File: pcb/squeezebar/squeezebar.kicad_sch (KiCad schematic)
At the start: 44 parts, among them J2 Conn_02x08_Counter_Clockwise, U1 Elite-C

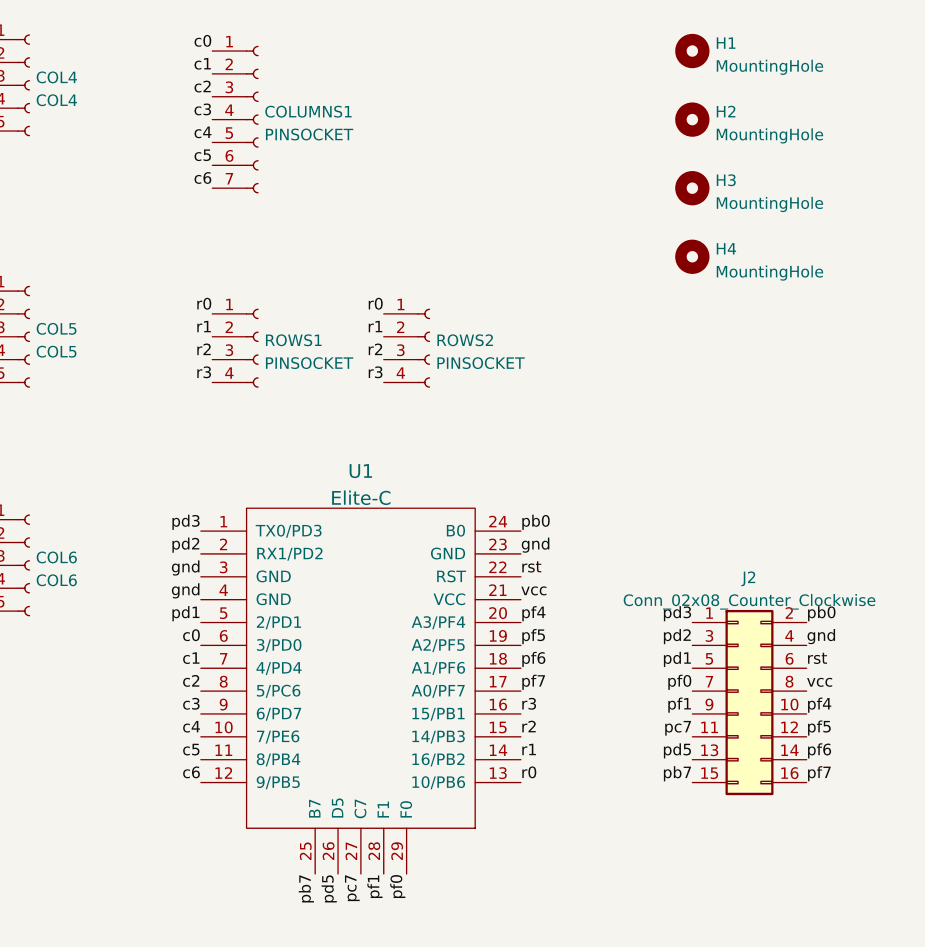
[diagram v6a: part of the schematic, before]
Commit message: Reassign pins; break out I²C & RST at the expense of 2 mounting holes
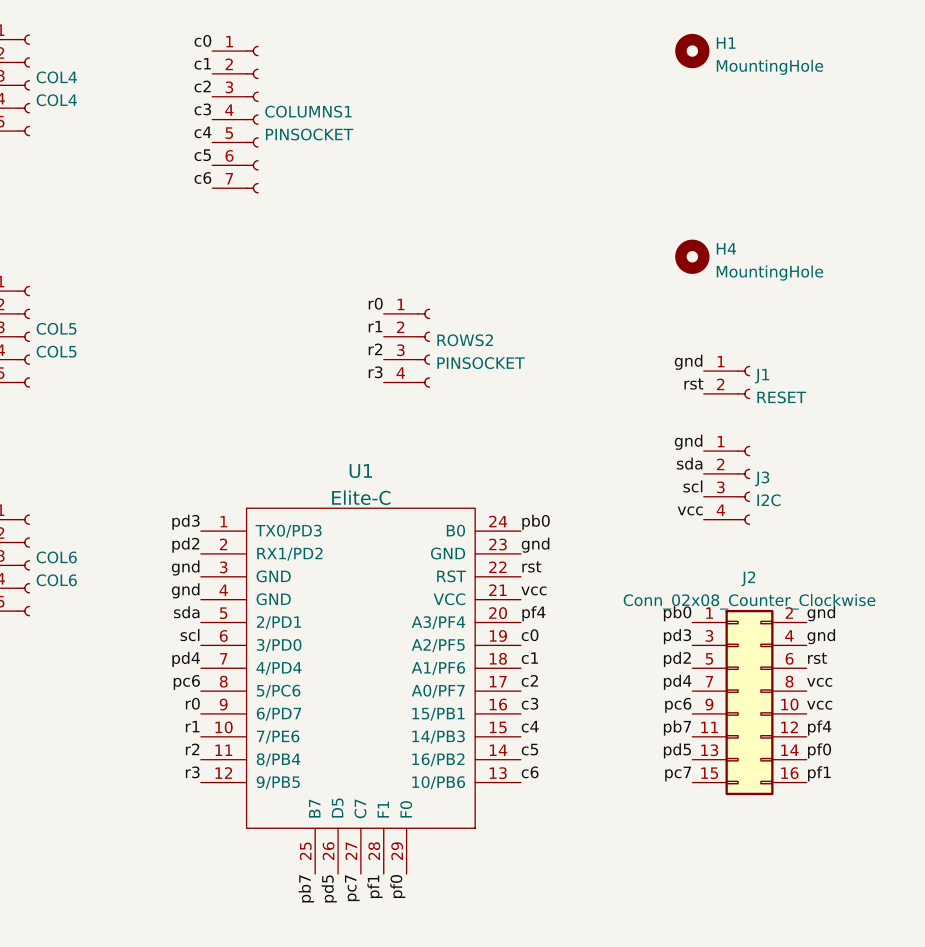
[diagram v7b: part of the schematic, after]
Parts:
- removed H2, H3: MountingHole, symbol Mechanical:MountingHole
- removed ROWS1: PINSOCKET, Library:PinSocket_1x04_P2.54mm_Vertical_LongPads, symbol Connector:Conn_01x04_Female
- added J1: RESET, Library:PinHeader_RST_1x02_P2.54mm_Vertical, symbol Connector:Conn_01x02_Female
- added J3: I2C, Library:PinHeader_I2C_1x04_P2.54mm_Vertical, symbol Connector:Conn_01x04_Female
- COL0, COL1, COL2, COL3, COL4, COL5, COL6: footprint Library:PinHeader_1x05_P2.54mm_Vertical -> Library:PinHeader_Col_1x05_P2.54mm_Vertical
- COLUMNS1: footprint Connector_PinHeader_2.54mm:PinHeader_1x07_P2.54mm_Vertical -> Library:PinHeader_COLS_1x07_P2.54mm_Vertical
- H1, H4: footprint (none) -> MountingHole:MountingHole_3.2mm_M3_DIN965
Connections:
- net c0: now also U1.19 (A2/PF5); no longer U1.6 (3/PD0)
- net c1: now also U1.18 (A1/PF6); no longer U1.7 (4/PD4)
- net c2: now also U1.17 (A0/PF7); no longer U1.8 (5/PC6)
- net c3: now also U1.16 (15/PB1); no longer U1.9 (6/PD7)
- net c4: now also U1.15 (14/PB3); no longer U1.10 (7/PE6)
- net c5: now also U1.14 (16/PB2); no longer U1.11 (8/PB4)
- net c6: now also U1.13 (10/PB6); no longer U1.12 (9/PB5)
- net gnd: now also J2.2 (Pin_2), J1.1 (Pin_1), J3.1 (Pin_1)
- net pb0: now also J2.1 (Pin_1); no longer J2.2 (Pin_2)
- net pb7: now also J2.11 (Pin_11); no longer J2.15 (Pin_15)
- net pc7: now also J2.15 (Pin_15); no longer J2.11 (Pin_11)
- net pd2: now also J2.5 (Pin_5); no longer J2.3 (Pin_3)
- net pd3: now also J2.3 (Pin_3); no longer J2.1 (Pin_1)
- net pf0: now also J2.14 (Pin_14); no longer J2.7 (Pin_7)
- net pf1: now also J2.16 (Pin_16); no longer J2.9 (Pin_9)
- net pf4: now also J2.12 (Pin_12); no longer J2.10 (Pin_10)
- net r0: now also U1.9 (6/PD7); no longer U1.13 (10/PB6)
- net r1: now also U1.10 (7/PE6); no longer U1.14 (16/PB2)
- net r2: now also U1.11 (8/PB4); no longer U1.15 (14/PB3)
- net r3: now also U1.12 (9/PB5); no longer U1.16 (15/PB1)
- net rst: now also J1.2 (Pin_2)
- net vcc: now also J2.10 (Pin_10), J3.4 (Pin_4)
- net pd1 renamed sda
- net sda: now also J3.2 (Pin_2); no longer J2.5 (Pin_5)
- removed net pf5: J2.12 (Pin_12), U1.19 (A2/PF5)
- removed net pf6: J2.14 (Pin_14), U1.18 (A1/PF6)
- removed net pf7: J2.16 (Pin_16), U1.17 (A0/PF7)
- new net pc6: J2.9 (Pin_9), U1.8 (5/PC6)
- new net pd4: J2.7 (Pin_7), U1.7 (4/PD4)
- new net scl: J3.3 (Pin_3), U1.6 (3/PD0)

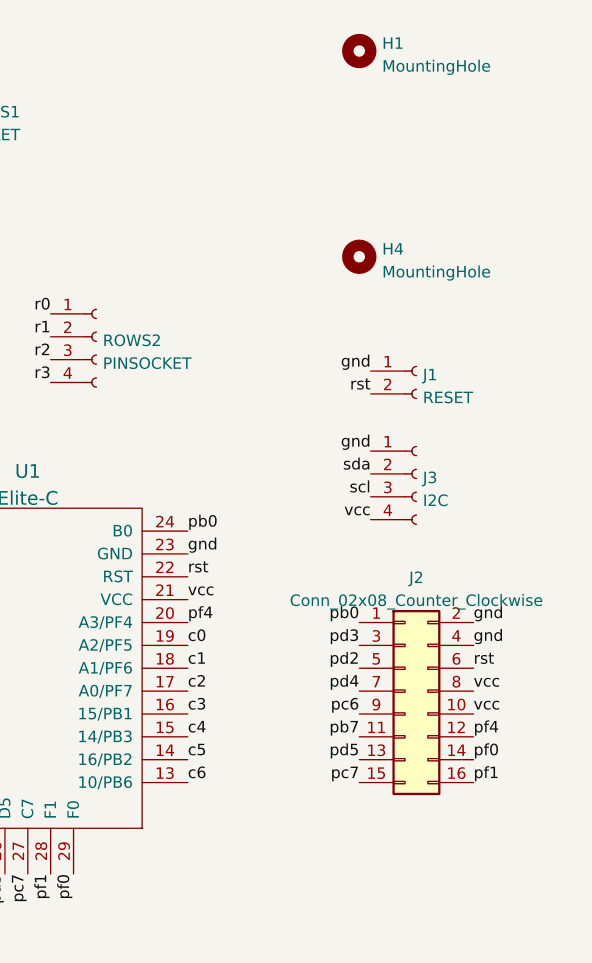
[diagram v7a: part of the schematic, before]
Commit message: Move mounting hole from under the MCU
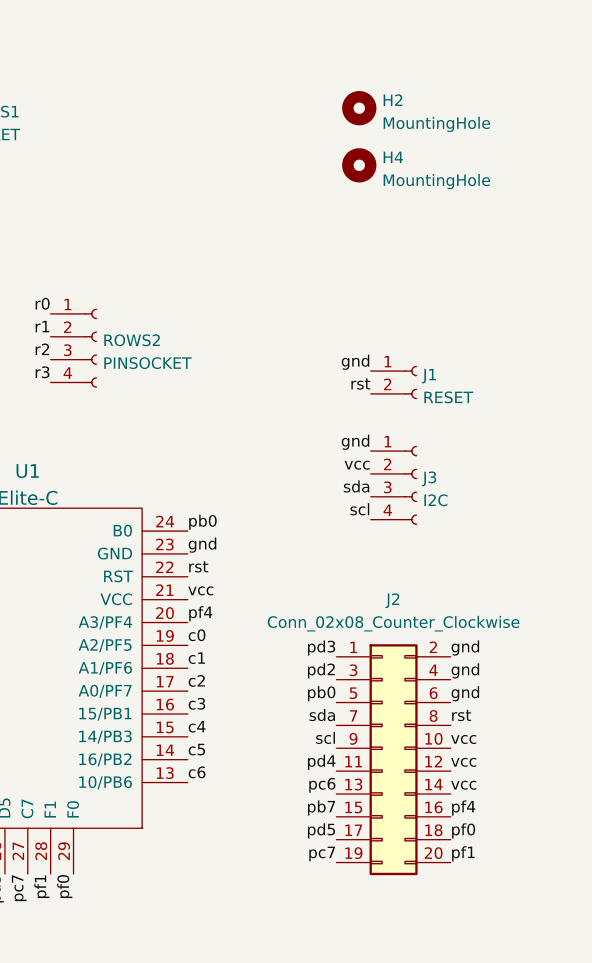
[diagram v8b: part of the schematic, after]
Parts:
- removed H1: MountingHole, MountingHole:MountingHole_3.2mm_M3_DIN965, symbol Mechanical:MountingHole
- added H2: MountingHole, MountingHole:MountingHole_3.2mm_M3_DIN965, symbol Mechanical:MountingHole
- J2: footprint Library:PinSocket_2x08_P2.54mm_Bespoke -> Connector_PinSocket_2.54mm:PinSocket_2x10_P2.54mm_Vertical; symbol Connector_Generic:Conn_02x08_Odd_Even -> Connector_Generic:Conn_02x10_Odd_Even
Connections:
- net gnd: now also J2.6 (Pin_6)
- net pb0: now also J2.5 (Pin_5); no longer J2.1 (Pin_1)
- net pb7: now also J2.15 (Pin_15); no longer J2.11 (Pin_11)
- net pc6: now also J2.13 (Pin_13); no longer J2.9 (Pin_9)
- net pc7: now also J2.19 (Pin_19); no longer J2.15 (Pin_15)
- net pd2: now also J2.3 (Pin_3); no longer J2.5 (Pin_5)
- net pd3: now also J2.1 (Pin_1); no longer J2.3 (Pin_3)
- net pd4: now also J2.11 (Pin_11); no longer J2.7 (Pin_7)
- net pd5: now also J2.17 (Pin_17); no longer J2.13 (Pin_13)
- net pf0: now also J2.18 (Pin_18); no longer J2.14 (Pin_14)
- net pf1: now also J2.20 (Pin_20); no longer J2.16 (Pin_16)
- net pf4: now also J2.16 (Pin_16); no longer J2.12 (Pin_12)
- net rst: now also J2.8 (Pin_8); no longer J2.6 (Pin_6)
- net scl: now also J2.9 (Pin_9), J3.4 (Pin_4); no longer J3.3 (Pin_3)
- net sda: now also J2.7 (Pin_7), J3.3 (Pin_3); no longer J3.2 (Pin_2)
- net vcc: now also J2.12 (Pin_12), J2.14 (Pin_14), J3.2 (Pin_2); no longer J2.8 (Pin_8), J3.4 (Pin_4)
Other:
- moved on the sheet: H4
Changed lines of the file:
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@@
     (stroke (width 0) (type default) (color 0 0 0 0))
   )
-  (label "pd5" (at 177.8 100.33 180)
-    (effects (font (size 1.27 1.27)) (justify right bottom))
+  (label "pd5" (at 175.26 109.22 180)
+    (effects (font (size 1.27 1.27)) (justify right bottom))
+  )
+  (label "gnd" (at 187.96 93.98 0)
+    (effects (font (size 1.27 1.27)) (justify left bottom))
   )
   (label "r3" (at 43.18 68.58 0)
     (effects (font (size 1.27 1.27)) (justify left bottom))
   )
+  (label "vcc" (at 187.96 99.06 0)
+    (effects (font (size 1.27 1.27)) (justify left bottom))
+  )
   (label "c0" (at 158.75 87.63 0)
     (effects (font (size 1.27 1.27)) (justify left bottom))
@@
     (effects (font (size 1.27 1.27)) (justify left bottom))
   )
-  (label "pc7" (at 177.8 102.87 180)
+  (label "pc7" (at 175.26 111.76 180)
     (effects (font (size 1.27 1.27)) (justify right bottom))
   )
@@
     (effects (font (size 1.27 1.27)) (justify left bottom))
   )
-  (label "pf0" (at 190.5 100.33 0)
+  (label "pf0" (at 187.96 109.22 0)
     (effects (font (size 1.27 1.27)) (justify left bottom))
   )
@@
     (effects (font (size 1.27 1.27)) (justify left bottom))
   )
-  (label "pd3" (at 177.8 87.63 180)
+  (label "pd3" (at 175.26 88.9 180)
     (effects (font (size 1.27 1.27)) (justify right bottom))
   )
@@
     (effects (font (size 1.27 1.27)) (justify left bottom))
   )
+  (label "scl" (at 179.07 73.66 180)
+    (effects (font (size 1.27 1.27)) (justify right bottom))
+  )
   (label "gnd" (at 123.19 82.55 180)
     (effects (font (size 1.27 1.27)) (justify right bottom))
@@
     (effects (font (size 1.27 1.27)) (justify left bottom))
   )
-  (label "vcc" (at 179.07 73.66 180)
-    (effects (font (size 1.27 1.27)) (justify right bottom))
-  )
-  (label "gnd" (at 190.5 85.09 0)
+  (label "vcc" (at 179.07 68.58 180)
+    (effects (font (size 1.27 1.27)) (justify right bottom))
+  )
+  (label "gnd" (at 187.96 88.9 0)
     (effects (font (size 1.27 1.27)) (justify left bottom))
   )
@@
     (effects (font (size 1.27 1.27)) (justify right bottom))
   )
-  (label "scl" (at 179.07 71.12 180)
+  (label "scl" (at 175.26 99.06 180)
     (effects (font (size 1.27 1.27)) (justify right bottom))
   )
@@
     (effects (font (size 1.27 1.27)) (justify right bottom))
   )
-  (label "pb7" (at 177.8 97.79 180)
-    (effects (font (size 1.27 1.27)) (justify right bottom))
-  )
-  (label "pd4" (at 177.8 92.71 180)
+  (label "pb7" (at 175.26 106.68 180)
+    (effects (font (size 1.27 1.27)) (justify right bottom))
+  )
+  (label "pd4" (at 175.26 101.6 180)
     (effects (font (size 1.27 1.27)) (justify right bottom))
   )
@@
     (effects (font (size 1.27 1.27)) (justify right bottom))
   )
-  (label "pf1" (at 190.5 102.87 0)
+  (label "pf1" (at 187.96 111.76 0)
     (effects (font (size 1.27 1.27)) (justify left bottom))
   )
@@
     (effects (font (size 1.27 1.27)) (justify left bottom))
   )
-  (label "vcc" (at 190.5 95.25 0)
+  (label "vcc" (at 187.96 104.14 0)
     (effects (font (size 1.27 1.27)) (justify left bottom))
   )
@@
     (effects (font (size 1.27 1.27)) (justify left bottom))
   )
-  (label "pc6" (at 177.8 95.25 180)
+  (label "pc6" (at 175.26 104.14 180)
     (effects (font (size 1.27 1.27)) (justify right bottom))
   )
@@
     (effects (font (size 1.27 1.27)) (justify left bottom))
   )
+  (label "sda" (at 179.07 71.12 180)
+    (effects (font (size 1.27 1.27)) (justify right bottom))
+  )
   (label "c4" (at 124.46 31.75 180)
     (effects (font (size 1.27 1.27)) (justify right bottom))
@@
     (effects (font (size 1.27 1.27)) (justify right bottom))
   )
-  (label "pd2" (at 177.8 90.17 180)
-    (effects (font (size 1.27 1.27)) (justify right bottom))
-  )
-  (label "vcc" (at 190.5 92.71 0)
+  (label "pd2" (at 175.26 91.44 180)
+    (effects (font (size 1.27 1.27)) (justify right bottom))
+  )
+  (label "vcc" (at 187.96 101.6 0)
     (effects (font (size 1.27 1.27)) (justify left bottom))
   )
@@
     (effects (font (size 1.27 1.27)) (justify left bottom))
   )
-  (label "pb0" (at 177.8 85.09 180)
+  (label "pb0" (at 175.26 93.98 180)
     (effects (font (size 1.27 1.27)) (justify right bottom))
   )
@@
     (effects (font (size 1.27 1.27)) (justify right bottom))
   )
-  (label "sda" (at 179.07 68.58 180)
+  (label "sda" (at 175.26 96.52 180)
     (effects (font (size 1.27 1.27)) (justify right bottom))
   )
@@
     (effects (font (size 1.27 1.27)) (justify left bottom))
   )
-  (label "pf4" (at 190.5 97.79 0)
+  (label "pf4" (at 187.96 106.68 0)
     (effects (font (size 1.27 1.27)) (justify left bottom))
   )
@@
     (effects (font (size 1.27 1.27)) (justify left bottom))
   )
-  (label "gnd" (at 190.5 87.63 0)
+  (label "gnd" (at 187.96 91.44 0)
     (effects (font (size 1.27 1.27)) (justify left bottom))
   )
@@
     (effects (font (size 1.27 1.27)) (justify left bottom))
   )
-  (label "rst" (at 190.5 90.17 0)
+  (label "rst" (at 187.96 96.52 0)
     (effects (font (size 1.27 1.27)) (justify left bottom))
   )
@@
     (pin "1")
     (pin "2")
-  )
-  (symbol (lib_id "Mechanical:MountingHole") (at 177.8 21.59 0) (unit 1)
-    (in_bom yes) (on_board yes) (fields_autoplaced)
-    (property "Reference" "H1" (id 0) (at 180.34 20.7553 0)
-      (effects (font (size 1.27 1.27)) (justify left))
-    )
-    (property "Value" "MountingHole" (id 1) (at 180.34 23.2922 0)
-      (effects (font (size 1.27 1.27)) (justify left))
-    )
-    (property "Footprint" "MountingHole:MountingHole_3.2mm_M3_DIN965" (id 2) (at 177.8 21.59 0)
-      (effects (font (size 1.27 1.27)) hide)
-    )
-    (property "Datasheet" "~" (id 3) (at 177.8 21.59 0)
-      (effects (font (size 1.27 1.27)) hide)
-    )
   )
   (symbol (lib_id "Connector:Conn_01x07_Female") (at 129.54 29.21 0) (unit 1)
@@
     (pin "2")
   )
-  (symbol (lib_id "Connector_Generic:Conn_02x08_Odd_Even") (at 182.88 92.71 0) (unit 1)
-    (in_bom yes) (on_board yes) (fields_autoplaced)
-    (property "Reference" "J2" (id 0) (at 184.15 80.1202 0))
-    (property "Value" "Conn_02x08_Counter_Clockwise" (id 1) (at 184.15 82.6571 0))
-    (property "Footprint" "Library:PinSocket_2x08_P2.54mm_Bespoke" (id 2) (at 182.88 92.71 0)
-      (effects (font (size 1.27 1.27)) hide)
-    )
-    (property "Datasheet" "~" (id 3) (at 182.88 92.71 0)
+  (symbol (lib_id "Connector_Generic:Conn_02x10_Odd_Even") (at 180.34 99.06 0) (unit 1)
+    (in_bom yes) (on_board yes)
+    (property "Reference" "J2" (id 0) (at 181.61 82.55 0))
+    (property "Value" "Conn_02x08_Counter_Clockwise" (id 1) (at 181.61 85.09 0))
+    (property "Footprint" "Connector_PinSocket_2.54mm:PinSocket_2x10_P2.54mm_Vertical" (id 2) (at 180.34 99.06 0)
+      (effects (font (size 1.27 1.27)) hide)
+    )
+    (property "Datasheet" "~" (id 3) (at 180.34 99.06 0)
       (effects (font (size 1.27 1.27)) hide)
     )
@@
     (pin "15")
     (pin "16")
-    (pin "2")
+    (pin "17")
+    (pin "18")
+    (pin "19")
+    (pin "2")
+    (pin "20")
     (pin "3")
     (pin "4")
@@
     (pin "2")
   )
+  (symbol (lib_id "Mechanical:MountingHole") (at 177.8 27.94 0) (unit 1)
+    (in_bom yes) (on_board yes) (fields_autoplaced)
+    (property "Reference" "H2" (id 0) (at 180.34 27.1053 0)
+      (effects (font (size 1.27 1.27)) (justify left))
+    )
+    (property "Value" "MountingHole" (id 1) (at 180.34 29.6422 0)
+      (effects (font (size 1.27 1.27)) (justify left))
+    )
+    (property "Footprint" "MountingHole:MountingHole_3.2mm_M3_DIN965" (id 2) (at 177.8 27.94 0)
+      (effects (font (size 1.27 1.27)) hide)
+    )
+    (property "Datasheet" "~" (id 3) (at 177.8 27.94 0)
+      (effects (font (size 1.27 1.27)) hide)
+    )
+  )
   (symbol (lib_id "Connector:Conn_01x05_Female") (at 57.15 104.14 0) (unit 1)
     (in_bom yes) (on_board yes) (fields_autoplaced)
@@
     (pin "2")
   )
-  (symbol (lib_id "Mechanical:MountingHole") (at 177.8 44.45 0) (unit 1)
-    (in_bom yes) (on_board yes) (fields_autoplaced)
-    (property "Reference" "H4" (id 0) (at 180.34 43.6153 0)
-      (effects (font (size 1.27 1.27)) (justify left))
-    )
-    (property "Value" "MountingHole" (id 1) (at 180.34 46.1522 0)
-      (effects (font (size 1.27 1.27)) (justify left))
-    )
-    (property "Footprint" "MountingHole:MountingHole_3.2mm_M3_DIN965" (id 2) (at 177.8 44.45 0)
-      (effects (font (size 1.27 1.27)) hide)
-    )
-    (property "Datasheet" "~" (id 3) (at 177.8 44.45 0)
+  (symbol (lib_id "Mechanical:MountingHole") (at 177.8 34.29 0) (unit 1)
+    (in_bom yes) (on_board yes) (fields_autoplaced)
+    (property "Reference" "H4" (id 0) (at 180.34 33.4553 0)
+      (effects (font (size 1.27 1.27)) (justify left))
+    )
+    (property "Value" "MountingHole" (id 1) (at 180.34 35.9922 0)
+      (effects (font (size 1.27 1.27)) (justify left))
+    )
+    (property "Footprint" "MountingHole:MountingHole_3.2mm_M3_DIN965" (id 2) (at 177.8 34.29 0)
+      (effects (font (size 1.27 1.27)) hide)
+    )
+    (property "Datasheet" "~" (id 3) (at 177.8 34.29 0)
       (effects (font (size 1.27 1.27)) hide)
     )
@@
       (reference "COLUMNS1") (unit 1) (value "PINSOCKET") (footprint "Library:PinHeader_COLS_1x07_P2.54mm_Vertical")
     )
-    (path "/4a7faed8-406c-419a-aaa0-2e6ca12fec45"
-      (reference "H1") (unit 1) (value "MountingHole") (footprint "MountingHole:MountingHole_3.2mm_M3_DIN965")
+    (path "/a153c5b4-271a-436f-8170-79e6f7572b9a"
+      (reference "H2") (unit 1) (value "MountingHole") (footprint "MountingHole:MountingHole_3.2mm_M3_DIN965")
     )
     (path "/e78d8360-845a-4e52-a48a-372ed98ff282"
@@
     )
     (path "/66a7b41e-febe-411e-979f-084594b3b8e3"
-      (reference "J2") (unit 1) (value "Conn_02x08_Counter_Clockwise") (footprint "Library:PinSocket_2x08_P2.54mm_Bespoke")
+      (reference "J2") (unit 1) (value "Conn_02x08_Counter_Clockwise") (footprint "Connector_PinSocket_2.54mm:PinSocket_2x10_P2.54mm_Vertical")
     )
     (path "/c11a625c-4549-4045-b782-5d761cd1ed70"
